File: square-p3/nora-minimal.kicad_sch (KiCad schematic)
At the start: 11 parts, among them J1 UP2-AH-1-TH, J2 SWD / 3V3, J3 GPIO / 3V3, U1 NORA-B106-00B, U2 XC6206P332MR-G, U3 USBLC6-2SC6

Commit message: Narrow P3 board, centre USB and add cyber dragon artwork and optional reset
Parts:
- added SW1: RESET (optional), Breakout:SW_PUSH_6mm, symbol Switch:SW_Push
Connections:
- net GND: now also SW1.2
- net RESET_N: now also SW1.1
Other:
- title: NORA-B106 Square P3 / SWD / twelve GPIOs / optional USB -> NORA-B106 Dragon P3.1 / SWD / 12 GPIO / optional USB

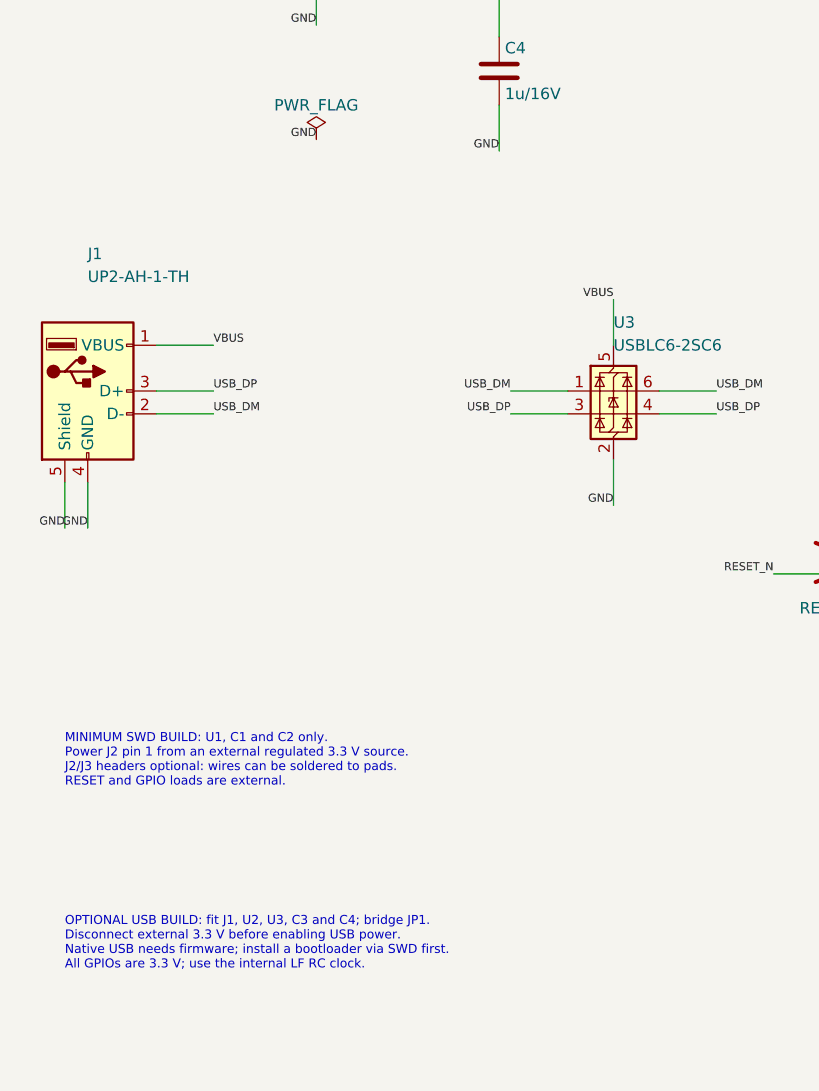
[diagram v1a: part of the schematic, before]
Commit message: Switch Dragon P3.2 to USB-C and restore four mounting holes
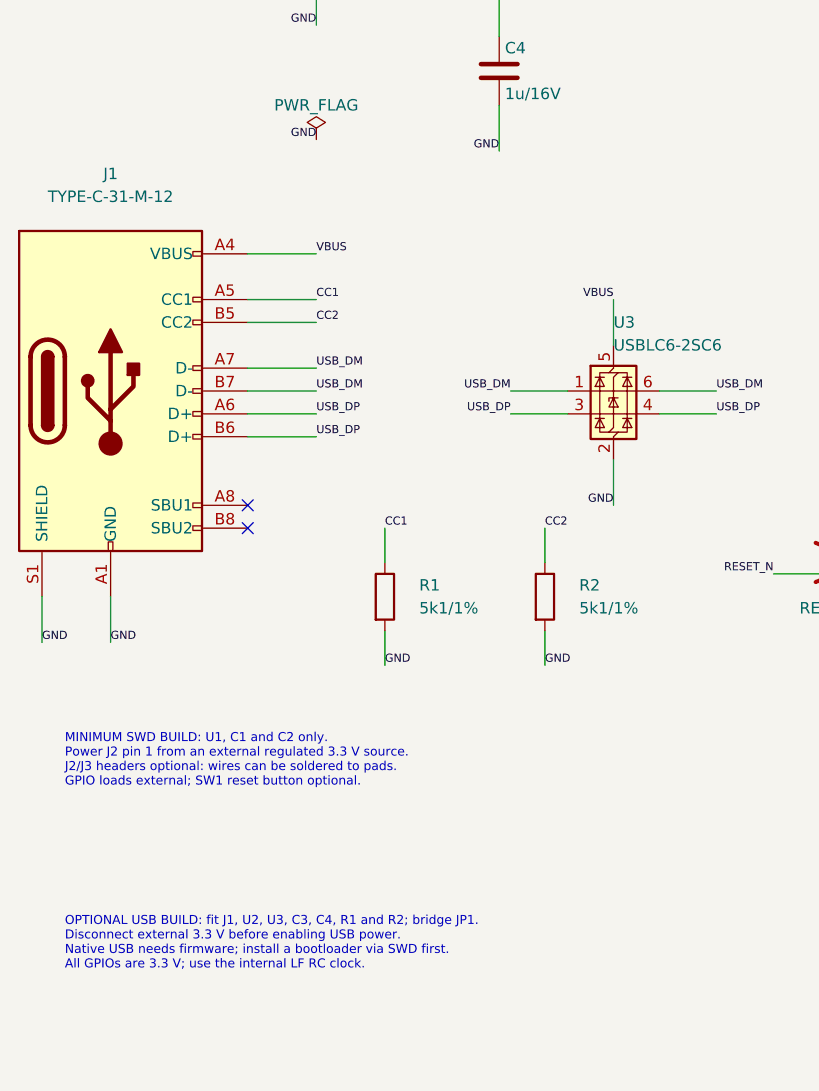
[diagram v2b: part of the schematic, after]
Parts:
- added R1, R2: 5k1/1%, Breakout:R_0805_2012Metric, symbol Device:R
- J1: value UP2-AH-1-TH -> TYPE-C-31-M-12; footprint Breakout:USB_A_UP2-AH-1-TH -> Breakout:USB_C_Receptacle_HRO_TYPE-C-31-M-12; symbol Connector:USB_A -> Connector:USB_C_Receptacle_USB2.0_16P
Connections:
- net GND: now also J1.A1 (GND), J1.A12 (GND), J1.B1 (GND), J1.B12 (GND), J1.S1 (SHIELD), R1.2, R2.2; no longer J1.4 (GND), J1.5 (Shield)
- net USB_DM: now also J1.A7 (D-), J1.B7 (D-); no longer J1.2 (D-)
- net USB_DP: now also J1.A6 (D+), J1.B6 (D+); no longer J1.3 (D+)
- net VBUS: now also J1.A4 (VBUS), J1.A9 (VBUS), J1.B4 (VBUS), J1.B9 (VBUS); no longer J1.1 (VBUS)
- new net CC1: J1.A5 (CC1), R1.1
- new net CC2: J1.B5 (CC2), R2.1
- no-connect marks 42 -> 44
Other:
- note added: "MINIMUM SWD BUILD: U1, C1 and C2 only. Power J2 pin 1 from an external regulated 3.3 V source. J2/J3 headers optional: wires can be soldered to pads. GPIO loads external; SW1 reset button optional."
- note added: "OPTIONAL USB BUILD: fit J1, U2, U3, C3, C4, R1 and R2; bridge JP1. Disconnect external 3.3 V before enabling USB power. Native USB needs firmware; install a bootloader via SWD first. All GPIOs are 3.3 V; use the internal LF RC clock."
- note removed: "MINIMUM SWD BUILD: U1, C1 and C2 only. Power J2 pin 1 from an external regulated 3.3 V source. J2/J3 headers optional: wires can be soldered to pads. RESET and GPIO loads are external."
- note removed: "OPTIONAL USB BUILD: fit J1, U2, U3, C3 and C4; bridge JP1. Disconnect external 3.3 V before enabling USB power. Native USB needs firmware; install a bootloader via SWD first. All GPIOs are 3.3 V; use the internal LF RC clock."
- title: NORA-B106 Dragon P3.1 / SWD / 12 GPIO / optional USB -> NORA-B106 Dragon P3.2 / USB-C / SWD / 12 GPIO
